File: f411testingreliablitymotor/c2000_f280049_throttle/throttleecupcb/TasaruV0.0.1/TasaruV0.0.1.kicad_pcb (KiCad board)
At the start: 4 copper layers, 100 x 86 mm, 161 parts, among them J1 Conn_02x05_Odd_EvenJtag, J2 173862-1, Q1 MMBT2222A, Q2 MMBT2222A, Q3 2N7002AQ, SW1 Push_Button, T1 MOT_PWM, T10 B_SPI_SIMO, T11 B_SPI_SOMI, T12 B_SPI_CLK, T13 B_SPI_CS, T14 +3v3, T2 MOT_PH, T3 +BATTP, T4 BRK_SENSE, T5 MOT_IPROPI2, T6 MOT_IPROPI1, T7 PGOOD, T8 CANTX, T9 CANRX, U1 SQJ147ELP-T1_GE3, U2 TPS1H100BQPWPRQ1, U3 DRV8873HPWPR, U4 F280049CPZS, U5 PSM33620S3QRDNRQ1, U6 SIT2024BA-S2-XXE-10.000000E, U7 PTCAN3404DRQ1, U8 AS5147U-HTSM, U9 TPS3702

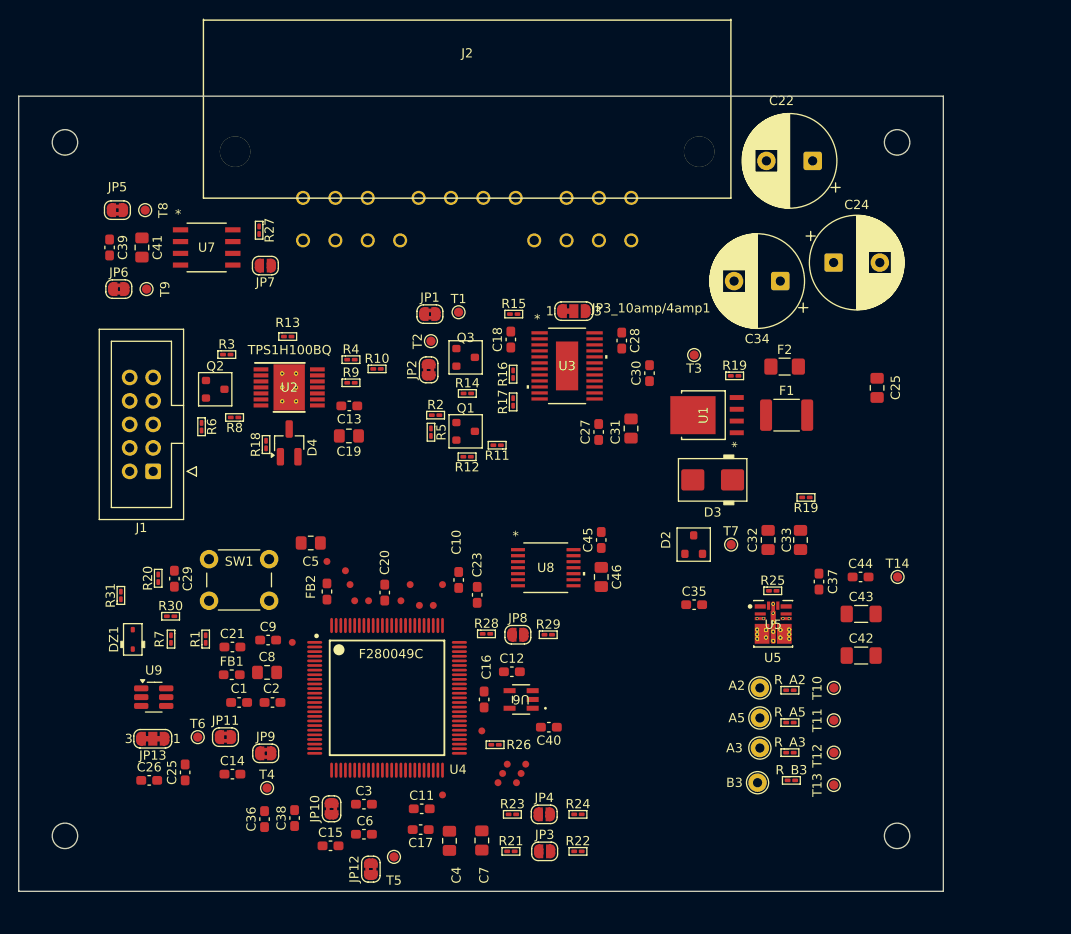
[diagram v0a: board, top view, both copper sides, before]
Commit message: Tasaru V0.0.1 PCB: layout/schematic revisions, production outputs, docs
- Update KiCad schematic and PCB layout (major routing/schematic rework)
- Add production outputs: gerbers, BOM, fabrication toolkit config, freerouting DSN
- Add DRC/ERC reports and JLC DFM analysis
- Add LAYOUT.md and MCU_PIN_FUNCTION_MAP.md docs; update FIRMWARE_PIN_MAP.md and HANDOFF.md
- Add Hindsight logo/arrow footprint libraries and fp-lib-table
- Add component datasheets (LMR38020-Q1, TCAN3404-Q1, TPS3702-Q1, DRV8873 supplement)
- Prune old KiCad backup zips, add current ones; remove stale lock files
- Ignore .history/ editor cache, *.lck, and stray personal PDFs via .gitignore

Co-Authored-By: Claude Fable 5 <noreply@anthropic.com>
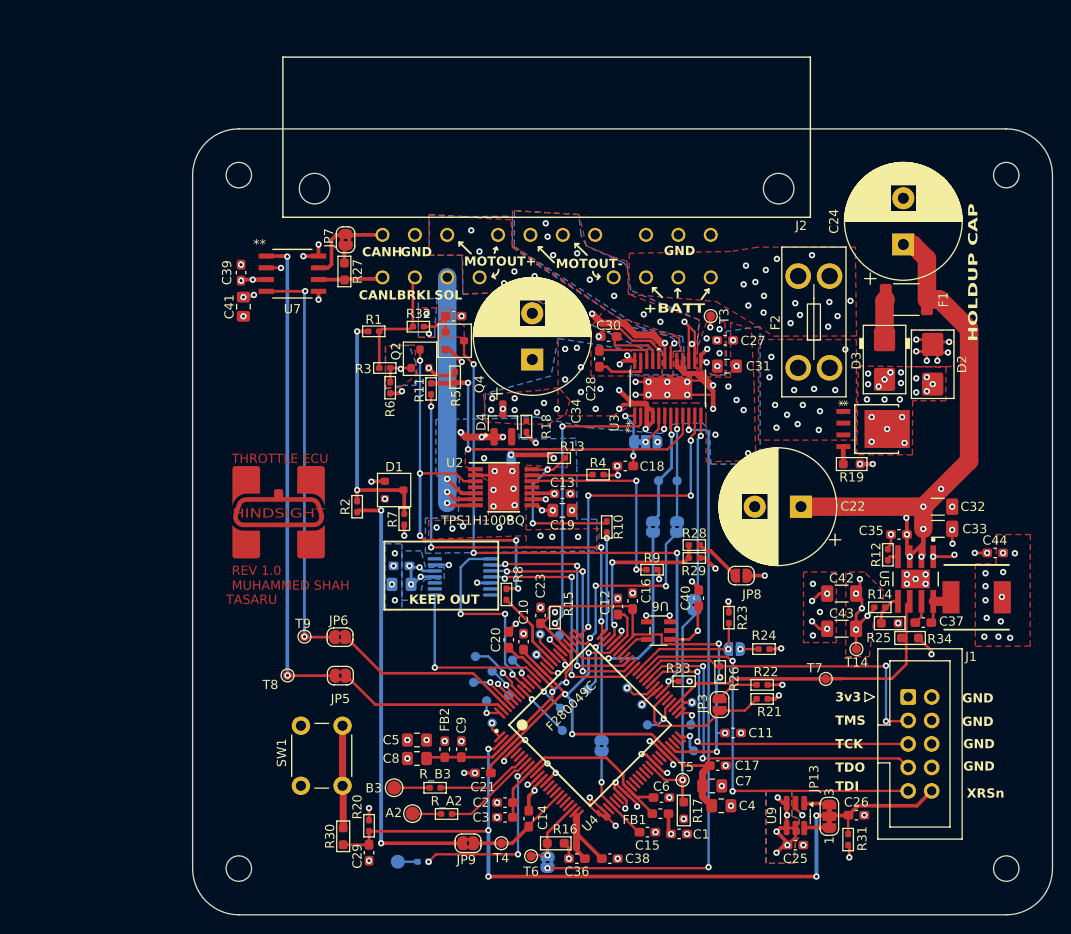
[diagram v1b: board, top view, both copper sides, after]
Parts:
- removed A5: SPARE_ADC_A5, TestPoint:TestPoint_THTPad_D2.0mm_Drill1.0mm
- removed the C25 at (108.0, 123.1)
- removed the C25 at (182.8, 81.5)
- removed DZ1: BZT52C3V3S, PCM_Diode_SMD_AKL:D_SOD-323
- removed IO17, IO18_X2, IO25, IO33: GPIO, PCM_SparkFun-Connector:TestPoint-0.75mm
- removed Q1: MMBT2222A, PCM_Package_TO_SOT_SMD_AKL:SOT-23
- removed Q3: 2N7002AQ, PCM_Package_TO_SOT_SMD_AKL:SOT-23
- removed the R19 at (175.1, 93.4)
- removed R_A5: 0ohm, PCM_Resistor_SMD_AKL:R_0201_0603Metric_Pad0.64x0.40mm_HandSolder
- added C25: 0.1uF, Capacitor_SMD:C_0603_1608Metric_Pad1.08x0.95mm_HandSolder, F.Cu at (174.0, 131.0)
- added C47: 0.1uF, Capacitor_SMD:C_0603_1608Metric_Pad1.08x0.95mm_HandSolder, F.Cu at (137.0, 73.8)
- added D1: BAV99, PCM_Package_TO_SOT_SMD_AKL:SOT-23, F.Cu at (130.6, 92.6)
- added HINDSIGHT: LOGO, hindsight_logo_gold, F.Cu at (118.1, 95.0)
- added L1: 10uH, PCM_SparkFun-Coil:Inductor_7.3x6.6mm, F.Cu at (193.6, 104.2)
- added Q4: MMBT2222A, PCM_Package_TO_SOT_SMD_AKL:SOT-23, F.Cu at (137.2, 76.5)
- added R32: 22k, PCM_Resistor_SMD_AKL:R_0402_1005Metric_Pad0.72x0.64mm_HandSolder, F.Cu at (133.2, 74.9)
- added R33: 4.7k, PCM_Resistor_SMD_AKL:R_0402_1005Metric_Pad0.72x0.64mm_HandSolder, F.Cu at (162.0, 113.3)
- added R34: 100k, PCM_Resistor_SMD_AKL:R_0603_1608Metric_Pad0.98x0.95mm_HandSolder, F.Cu at (186.4, 108.6)
- A2, B3: footprint TestPoint:TestPoint_THTPad_D2.0mm_Drill1.0mm -> TestPoint:TestPoint_Pad_D1.5mm
- A3: footprint TestPoint:TestPoint_THTPad_D2.0mm_Drill1.0mm -> TestPoint:TestPoint_Pad_D1.5mm; moved to B.Cu
- C14, C15: value 0.1uF -> 0.01uF
- C22, C24, C34: footprint Capacitor_THT:CP_Radial_D10.0mm_P5.00mm -> PCM_Capacitor_THT_US_AKL_Double:CP_Radial_D12.5mm_P5.00mm
- C32: value 10uF -> 22uF; footprint Capacitor_SMD:C_0805_2012Metric_Pad1.18x1.45mm_HandSolder -> Capacitor_SMD:C_1206_3216Metric_Pad1.33x1.80mm_HandSolder
- C33: value 10uF -> 0.1uF; footprint Capacitor_SMD:C_0805_2012Metric_Pad1.18x1.45mm_HandSolder -> Capacitor_SMD:C_1206_3216Metric_Pad1.33x1.80mm_HandSolder
- C35: value 0.1uF -> 4.7uF
- C37, C44: value 2.2uF -> 0.1uF
- C45, C46, JP1, JP10, JP11, JP12, JP2, JP3_10amp/4amp1, JP4, T1, T2, U8: moved to B.Cu
- D2: footprint PCM_Package_TO_SOT_SMD_AKL:SOT-23 -> PCM_Diode_SMD_AKL:D_SMB_TVS
- F2: footprint Fuse:Fuse_1206_3216Metric_Pad1.42x1.75mm_HandSolder -> PCM_Fuse_AKL:Fuseholder_Blade_Mini_Keystone_3568
- IO12: renamed from IO2; footprint PCM_SparkFun-Connector:TestPoint-0.75mm -> TestPoint:TestPoint_Pad_D1.0mm; moved to B.Cu
- IO13, IO14, IO15, IO16, IO22_SW1, IO23_SW1, IO26, IO27, IO28, IO29, IO34, IO39, IO40: footprint PCM_SparkFun-Connector:TestPoint-0.75mm -> TestPoint:TestPoint_Pad_D1.0mm; moved to B.Cu
- IO6: renamed from IO1; footprint PCM_SparkFun-Connector:TestPoint-0.75mm -> TestPoint:TestPoint_Pad_D1.0mm; moved to B.Cu
- JP7: footprint Jumper:SolderJumper-2_P1.3mm_Open_RoundedPad1.0x1.5mm -> Jumper:SolderJumper-2_P1.3mm_Bridged2Bar_RoundedPad1.0x1.5mm
- R1, R15, R5: value 100k -> 10k; footprint PCM_Resistor_SMD_AKL:R_0201_0603Metric_Pad0.64x0.40mm_HandSolder -> PCM_Resistor_SMD_AKL:R_0402_1005Metric_Pad0.72x0.64mm_HandSolder
- R10, R11, R13, R14, R18, R20, R21, R22, R23, R24, R26, R28, R29, R3, R31, R4, R6, R8, R9: footprint PCM_Resistor_SMD_AKL:R_0201_0603Metric_Pad0.64x0.40mm_HandSolder -> PCM_Resistor_SMD_AKL:R_0402_1005Metric_Pad0.72x0.64mm_HandSolder
- R12: value 100k -> 64.9k; footprint PCM_Resistor_SMD_AKL:R_0201_0603Metric_Pad0.64x0.40mm_HandSolder -> PCM_Resistor_SMD_AKL:R_0402_1005Metric_Pad0.72x0.64mm_HandSolder
- R16, R17, R19, R27, R30: footprint PCM_Resistor_SMD_AKL:R_0201_0603Metric_Pad0.64x0.40mm_HandSolder -> PCM_Resistor_SMD_AKL:R_0603_1608Metric_Pad0.98x0.95mm_HandSolder
- R2: value 22k -> 1k; footprint PCM_Resistor_SMD_AKL:R_0201_0603Metric_Pad0.64x0.40mm_HandSolder -> PCM_Resistor_SMD_AKL:R_0402_1005Metric_Pad0.72x0.64mm_HandSolder
- R25: value 100k -> 43.2k; footprint PCM_Resistor_SMD_AKL:R_0201_0603Metric_Pad0.64x0.40mm_HandSolder -> PCM_Resistor_SMD_AKL:R_0603_1608Metric_Pad0.98x0.95mm_HandSolder
- R7: value 22k -> 2.2k; footprint PCM_Resistor_SMD_AKL:R_0201_0603Metric_Pad0.64x0.40mm_HandSolder -> PCM_Resistor_SMD_AKL:R_0402_1005Metric_Pad0.72x0.64mm_HandSolder
- R_A2, R_B3: value 0ohm -> 0.1mohm; footprint PCM_Resistor_SMD_AKL:R_0201_0603Metric_Pad0.64x0.40mm_HandSolder -> PCM_Resistor_SMD_AKL:R_0402_1005Metric_Pad0.72x0.64mm_HandSolder
- R_A3: footprint PCM_Resistor_SMD_AKL:R_0201_0603Metric_Pad0.64x0.40mm_HandSolder -> PCM_Resistor_SMD_AKL:R_0402_1005Metric_Pad0.72x0.64mm_HandSolder; moved to B.Cu
- T10: value B_SPI_SIMO -> A_SPI_SIMO; moved to B.Cu
- T11: value B_SPI_SOMI -> A_SPI_CLK; moved to B.Cu
- T12: value B_SPI_CLK -> A_SPI_SOMI; moved to B.Cu
- T13: value B_SPI_CS -> A_SPI_CS; moved to B.Cu
- U5: value PSM33620S3QRDNRQ1 -> PLMR38020FSQDDARQ1; footprint TPSM33620-Q1:RDN0011B-MFG -> lmr38020:DDA0008E-IPC_A
- moved J1 85.2 mm to (186.2, 115.0), turned to 0 degrees
- moved R31 83.0 mm to (179.7, 130.4), turned to -90 degrees
- moved C26 76.6 mm to (180.6, 127.8), turned to 180 degrees
- moved JP13 73.7 mm to (177.7, 127.9), turned to 90 degrees
- moved U9 70.6 mm to (174.0, 127.8), turned to -90 degrees
- moved JP5 55.8 mm to (124.8, 112.7), turned to 180 degrees
- moved T8 52.6 mm to (119.1, 112.6), turned to 90 degrees
- moved R16 50.9 mm to (148.1, 130.8), turned to 0 degrees
- moved R14 50.3 mm to (183.1, 105.3)
- moved C1 49.7 mm to (161.4, 129.8)
- moved FB1 48.7 mm to (159.4, 127.6), turned to 180 degrees
- moved R17 47.9 mm to (161.9, 127.3), turned to -90 degrees
- moved R12 46.7 mm to (184.0, 99.6), turned to 90 degrees
- moved JP12 45.2 mm to (163.1, 105.0)
- moved JP6 44.6 mm to (124.8, 108.5), turned to 180 degrees
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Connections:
- net /<NO NET> renamed /10Mhz_Ocillator_Out
- net Net-(D4-A) renamed /SOL_CLEAN_GND
- net Net-(U5-EN) renamed /Vin
- net VDD renamed 1V2_Core
- C37 pad 1: GND -> Net-(U5-SW)
- C37 pad 2: Net-(U5-VCC) -> Net-(U5-BOOT)
- C45 pad 2: Net-(U8-VDD) -> +3V3
- C46 pad 2: Net-(U8-VDD) -> +3V3
- F2 pad 1: Net-(F2-Pad1) -> /15aFusedBATT
- IO12 pad 1: Net-(U4A-GPIO03) -> Net-(U4A-GPIO12)
- IO6 pad 1: Net-(U4A-GPIO01) -> Net-(U4A-GPIO06)
- J2 pad 15: /MOT_OUT- -> /MOT_OUT+
- J2 pad 16: /+SOL -> /MOT_OUT+
- J2 pad 4: /MOT_OUT+ -> /MOT_OUT-
- J2 pad 6: /MOT_OUT+ -> /+SOL
- JP9 pad 1: /BRK_SENSE -> Net-(JP9-A)
- R11 pad 2: Net-(Q1-C) -> /DISABLE
- R12 pad 1: Net-(Q1-C) -> Net-(U5-RT_SYNC)
- R14 pad 2: /DISABLE -> Net-(U5-FB)
- R2 pad 1: Net-(Q1-B) -> Net-(JP9-A)
- R2 pad 2: /12V_BRAKEIN -> /BRK_SENSE
- R25 pad 1: /PGOOD -> Net-(U5-FB)
- R25 pad 2: Net-(U5-VCC) -> GND
- R5 pad 1: Net-(Q1-B) -> /DISABLE
- T10 pad 1: /B_SPI_SIMO -> /A_SPI_SIMO
- T11 pad 1: /B_SPI_SOMI -> /A_SPI_CLK
- T12 pad 1: /B_SPI_CLK -> /A_SPI_SOMI
- T13 pad 1: /B_SPI_CS -> /A_SPI_CS
- T5 pad 1: Net-(JP12-B) -> /MOT_IPROPI2
- T6 pad 1: Net-(JP11-B) -> /MOT_IPROPI1
- U1 pad 1: Net-(F2-Pad1) -> /15aFusedBATT
- U1 pad 2: +BATT -> /15aFusedBATT
- U1 pad 3: +BATT -> /15aFusedBATT
- U3 pad 10: /MOT_IPROPI1 -> Net-(JP11-B)
- U3 pad 12: /MOT_IPROPI2 -> Net-(JP12-B)
- U3 pad EPAD: (no net) -> GND
- U4 pad 23: Net-(JP11-B) -> /MOT_IPROPI1
- U4 pad 35: /A5 -> unconnected-(U4C-A5-Pad35)
- U4 pad 41: Net-(JP12-B) -> /MOT_IPROPI2
- U4 pad 51: /nFault -> Net-(U4A-GPIO12)
- U4 pad 52: /SPI_CS -> /A_SPI_CS
- U4 pad 53: Net-(U4B-GPIO33) -> /PGOOD
- U4 pad 55: Net-(U4A-GPIO17) -> unconnected-(U4A-GPIO17-Pad55)
- U4 pad 57: Net-(U4A-GPIO25) -> /BRK_SW
- U4 pad 65: /B_SPI_SIMO -> /SPI_MOSI
- U4 pad 66: /B_SPI_SOMI -> /SPI_MISO
- U4 pad 67: /B_SPI_CLK -> /SPI_CLK
- U4 pad 68: Net-(U4A-GPIO18_X2) -> unconnected-(U4A-GPIO18_X2-Pad68)
- U4 pad 74: /SPI_MOSI -> /A_SPI_SIMO
- U4 pad 75: /SENSOR_PWM -> /MOT_DISABLE
- U4 pad 76: Net-(U4A-GPIO03) -> /MOT_nSLEEP
- U4 pad 78: Net-(U4A-GPIO01) -> /nFault
- U4 pad 89: /MOT_nSLEEP -> /SENSOR_PWM
- U4 pad 90: /SPI_CLK -> /A_SPI_CLK
- U4 pad 92: /B_SPI_CS -> /SPI_CS
- U4 pad 93: /SPI_MISO -> /A_SPI_SOMI
- U4 pad 97: /MOT_DISABLE -> Net-(U4A-GPIO06)
- U5 pad 1: /PGOOD -> GND
- U5 pad 4: +3V3 -> Net-(U5-RT_SYNC)
- U5 pad 5: unconnected-(U5-SW-Pad5) -> Net-(U5-FB)
- U5 pad 6: unconnected-(U5-SW-Pad6) -> /PGOOD
- U5 pad 7: unconnected-(U5-BOOT-Pad7) -> Net-(U5-BOOT)
- U5 pad 8: Net-(U5-VCC) -> Net-(U5-SW)
- U5 pad 9: +3V3 -> GND
- U8 pad 11: Net-(U8-VDD) -> +3V3
- U8 pad 12: Net-(U8-VDD) -> +3V3
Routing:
- net GND: track 0.00 -> 137.7 mm, vias 0 -> 138
- net /XRSn: track 0.00 -> 90.8 mm, vias 0 -> 5
- net VDDIO: track 0.00 -> 79.3 mm, vias 0 -> 6
- net /BRK_SW: track 0.00 -> 74.8 mm, vias 0 -> 4
- net Net-(JP11-B): track 0.00 -> 68.3 mm, vias 0 -> 3
- net /Vin: track 0.00 -> 62.2 mm, vias 0 -> 7
- net 1V2_Core: track 0.00 -> 58.9 mm, vias 0 -> 3
- net +3V3: track 0.00 -> 55.2 mm, vias 0 -> 46
- net Net-(JP5-B): track 0.00 -> 52.7 mm, vias 0 -> 2
- net Net-(JP9-A): track 0.00 -> 47.4 mm, vias 0 -> 2
- net /PGOOD: track 0.00 -> 45.7 mm
- net Net-(JP6-B): track 0.00 -> 44.8 mm, vias 0 -> 2
- net /MOT_DISABLE: track 0.00 -> 44.4 mm, vias 0 -> 4
- net /TDI: track 0.00 -> 43.9 mm, vias 0 -> 2
- net /IN_SOL_DRIVER: track 0.00 -> 43.7 mm, vias 0 -> 5
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- added copper zone on B.Cu, net +3V3
- added copper zone on F.Cu, net +3V3
- added copper zone on In2.Cu, net +3V3
- added copper zone on F.Cu, net +BATT
- added copper zone on In2.Cu, net +BATT
- added copper zone on F.Cu, net /+BATTPROTECTED
- added copper zone on In2.Cu, net /+BATTPROTECTED
- added copper zone on F.Cu, net /15aFusedBATT
- added copper zone on In2.Cu, net /15aFusedBATT
- added copper zone on B.Cu, net /MOT_OUT+
- added copper zone on F.Cu, net /MOT_OUT+
- added copper zone on B.Cu, net /MOT_OUT-
- added copper zone on F.Cu, net /MOT_OUT-
- added copper zone on B.Cu, net /SOL_CLEAN_GND
- added copper zone on F.Cu, net /SOL_CLEAN_GND
- added copper zone on In1.Cu, net /SOL_CLEAN_GND
- added copper zone on In2.Cu, net /Vin
- added copper zone on B.Cu, net GND
- added copper zone on F.Cu, net GND
- added copper zone on In1.Cu, net GND
- added copper zone on B.Cu, net Net-(Q2-B)
- added copper zone on F.Cu, net Net-(Q2-B)
- added copper zone on B.Cu, net Net-(Q4-B)
- added copper zone on F.Cu, net Net-(Q4-B)
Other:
- board size 100 x 86 mm -> 93 x 85 mm
- board text added: "+BATT"
- board text added: "+SOL"
- board text added: "12V_BRAKEIN"
- board text added: "3v3"
- board text added: "BRKI"
- board text added: "CANH"
- board text added: "CANL"
- board text added: "GND"
- board text added: "HOLDUP CAP"
- board text added: "KEEP OUT"
- board text added: "MOTOUT+"
- board text added: "MOTOUT-"
- board text added: "MOT_OUT+"
- board text added: "MOT_OUT-"
- board text added: "REV 1.0 MUHAMMED SHAH"
- board text added: "SOL"
- board text added: "TASARU"
- board text added: "TCK"
- board text added: "TDI"
- board text added: "TDO"
- board text added: "THROTTLE ECU"
- board text added: "TMS"
- board text added: "XRSn"
